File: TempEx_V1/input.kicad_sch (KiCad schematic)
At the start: 7 parts, among them J1 Conn_01x02, U1 MAX31865xTP

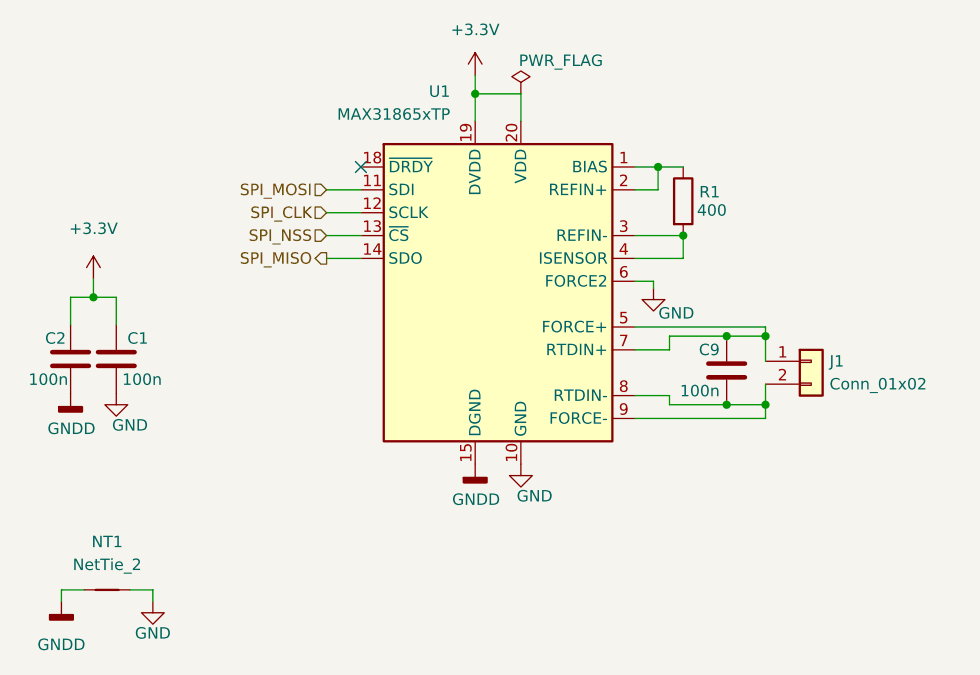
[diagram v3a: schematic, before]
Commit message: Updated GND
All GNDD switched to GND
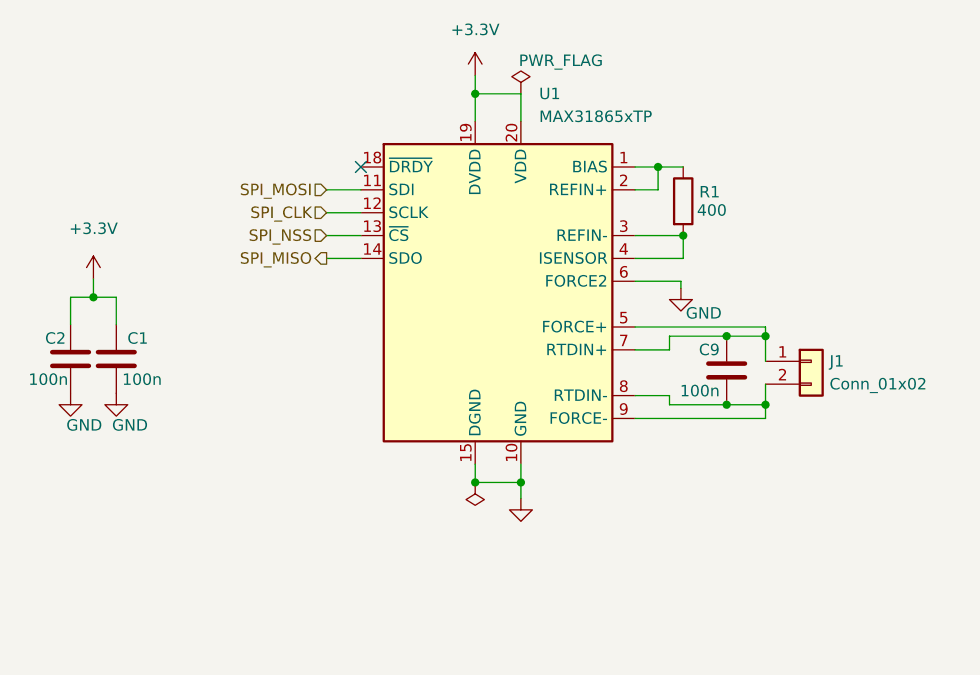
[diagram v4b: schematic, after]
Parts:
- removed NT1: NetTie_2, symbol Device:NetTie_2
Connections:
- net GNDD is gone; now on net GND: C2.2, U1.15 (DGND)

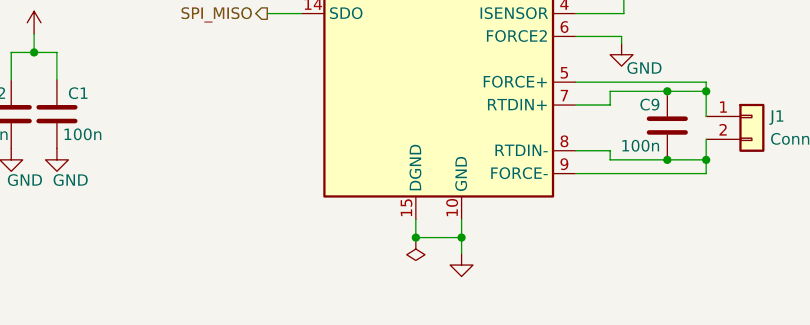
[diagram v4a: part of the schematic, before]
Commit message: Change from 2 layers to 4
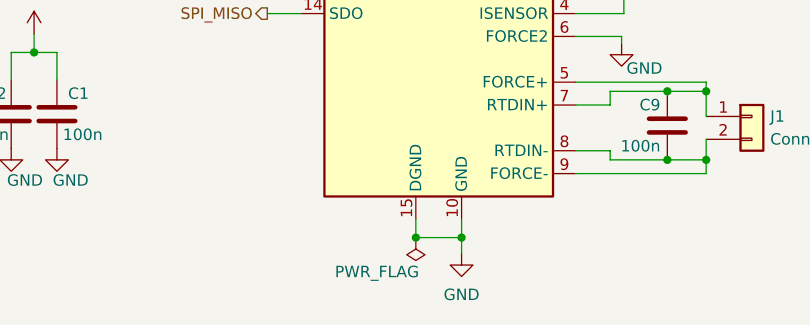
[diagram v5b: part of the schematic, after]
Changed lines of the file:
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@@
       (effects (font (size 1.27 1.27)) hide)
     )
-    (property "Value" "" (id 1) (at 182.118 123.19 0))
+    (property "Value" "GND" (id 1) (at 182.118 123.19 0))
     (property "Footprint" "" (id 2) (at 182.118 118.618 0)
       (effects (font (size 1.27 1.27)) hide)
@@
       (effects (font (size 1.27 1.27)) hide)
     )
-    (property "Value" "" (id 1) (at 172.72 120.65 0))
+    (property "Value" "PWR_FLAG" (id 1) (at 172.72 120.65 0))
     (property "Footprint" "" (id 2) (at 177.038 116.84 0)
       (effects (font (size 1.27 1.27)) hide)

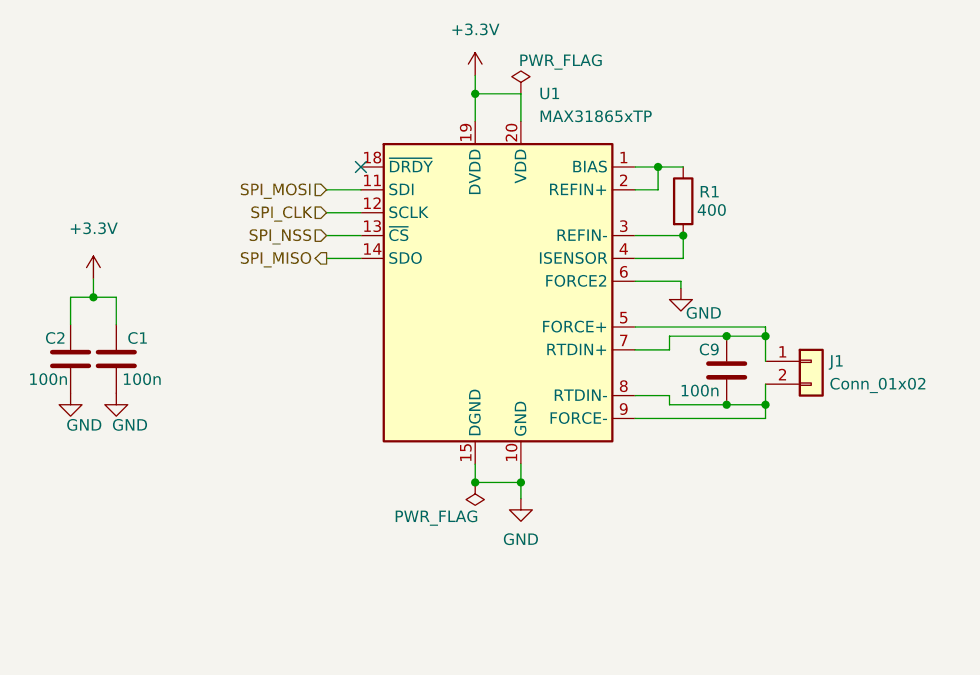
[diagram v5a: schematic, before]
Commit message: Layer change + 4 pin setup + stitching
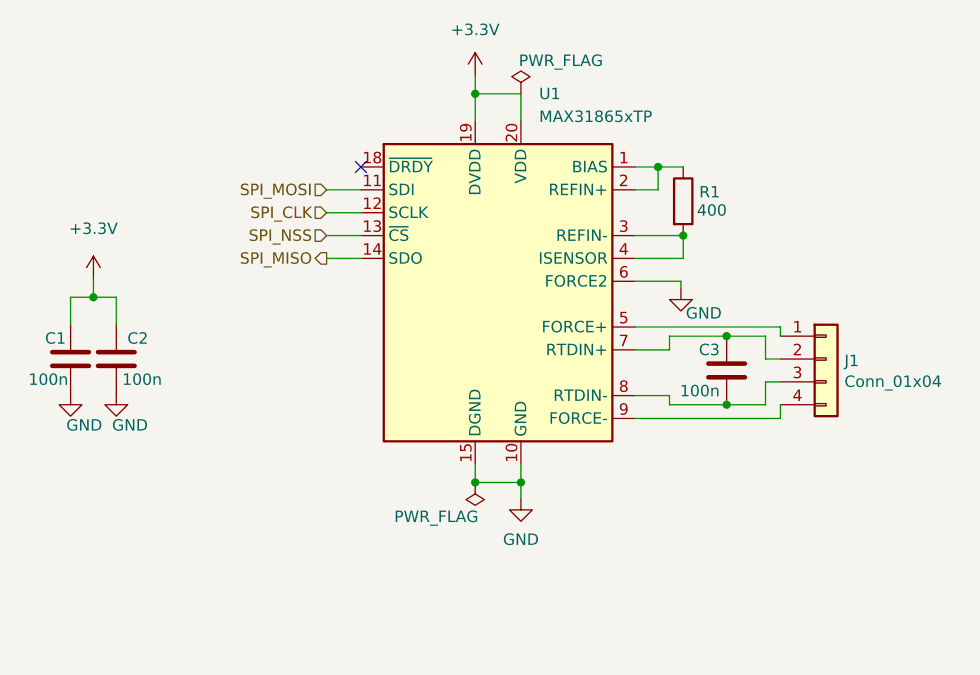
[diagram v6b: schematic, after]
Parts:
- removed J1: Conn_01x02, Connector_Molex:Molex_SL_171971-0002_1x02_P2.54mm_Vertical, symbol Connector_Generic:Conn_01x02
- added J1: Conn_01x04, TXV_Library_Footprints:TE_M12_4_Pin_PCB, symbol Connector_Generic:Conn_01x04
- renumbered C2 to C1, C1 to C2, C9 to C3
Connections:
- net at C3.1, U1.7 (RTDIN+): now also J1.2 (Pin_2); no longer U1.5 (FORCE+)
- net at C3.2, U1.8 (RTDIN-): now also J1.3 (Pin_3); no longer U1.9 (FORCE-)
- new net: J1.1 (Pin_1), U1.5 (FORCE+)
- new net: J1.4 (Pin_4), U1.9 (FORCE-)
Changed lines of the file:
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@@
   (junction (at 204.978 108.204) (diameter 0) (color 0 0 0 0)
   )
-  (junction (at 209.296 108.204) (diameter 0) (color 0 0 0 0)
-  )
-  (junction (at 209.296 100.584) (diameter 0) (color 0 0 0 0)
-  )
   (junction (at 177.038 116.84) (diameter 0) (color 0 0 0 0)
   )
@@
   )
   (no_connect (at 164.338 81.788))
-  (wire (pts (xy 209.296 109.728) (xy 209.296 108.204))
-    (stroke (width 0) (type default) (color 0 0 0 0))
-  )
   (wire (pts (xy 199.898 94.488) (xy 199.898 95.25))
     (stroke (width 0) (type default) (color 0 0 0 0))
@@
     (stroke (width 0) (type default) (color 0 0 0 0))
   )
-  (wire (pts (xy 194.818 99.568) (xy 209.296 99.568))
+  (wire (pts (xy 194.818 99.568) (xy 210.947 99.568))
     (stroke (width 0) (type default) (color 0 0 0 0))
   )
@@
     (stroke (width 0) (type default) (color 0 0 0 0))
   )
+  (wire (pts (xy 209.296 103.124) (xy 210.947 103.124))
+    (stroke (width 0) (type default) (color 0 0 0 0))
+  )
   (wire (pts (xy 194.818 81.788) (xy 197.358 81.788))
     (stroke (width 0) (type default) (color 0 0 0 0))
@@
     (stroke (width 0) (type default) (color 0 0 0 0))
   )
+  (wire (pts (xy 209.296 105.664) (xy 209.296 108.204))
+    (stroke (width 0) (type default) (color 0 0 0 0))
+  )
   (wire (pts (xy 177.038 116.84) (xy 182.118 116.84))
     (stroke (width 0) (type default) (color 0 0 0 0))
   )
-  (wire (pts (xy 209.296 100.584) (xy 209.296 103.378))
-    (stroke (width 0) (type default) (color 0 0 0 0))
-  )
   (wire (pts (xy 177.038 71.628) (xy 177.038 73.66))
     (stroke (width 0) (type default) (color 0 0 0 0))
@@
     (stroke (width 0) (type default) (color 0 0 0 0))
   )
+  (wire (pts (xy 210.947 100.584) (xy 210.947 99.568))
+    (stroke (width 0) (type default) (color 0 0 0 0))
+  )
   (wire (pts (xy 198.628 108.204) (xy 204.978 108.204))
     (stroke (width 0) (type default) (color 0 0 0 0))
@@
     (stroke (width 0) (type default) (color 0 0 0 0))
   )
-  (wire (pts (xy 209.296 99.568) (xy 209.296 100.584))
+  (wire (pts (xy 194.818 109.728) (xy 210.947 109.728))
+    (stroke (width 0) (type default) (color 0 0 0 0))
+  )
+  (wire (pts (xy 209.296 100.584) (xy 209.296 103.124))
     (stroke (width 0) (type default) (color 0 0 0 0))
   )
@@
     (stroke (width 0) (type default) (color 0 0 0 0))
   )
-  (wire (pts (xy 209.296 105.918) (xy 209.296 108.204))
-    (stroke (width 0) (type default) (color 0 0 0 0))
-  )
   (wire (pts (xy 204.978 100.584) (xy 209.296 100.584))
     (stroke (width 0) (type default) (color 0 0 0 0))
@@
     (stroke (width 0) (type default) (color 0 0 0 0))
   )
+  (wire (pts (xy 210.947 105.664) (xy 209.296 105.664))
+    (stroke (width 0) (type default) (color 0 0 0 0))
+  )
   (wire (pts (xy 182.118 116.84) (xy 182.118 114.808))
     (stroke (width 0) (type default) (color 0 0 0 0))
@@
     (stroke (width 0) (type default) (color 0 0 0 0))
   )
+  (wire (pts (xy 210.947 108.204) (xy 210.947 109.728))
+    (stroke (width 0) (type default) (color 0 0 0 0))
+  )
   (wire (pts (xy 198.628 100.584) (xy 204.978 100.584))
     (stroke (width 0) (type default) (color 0 0 0 0))
   )
   (wire (pts (xy 198.628 108.204) (xy 198.628 107.188))
-    (stroke (width 0) (type default) (color 0 0 0 0))
-  )
-  (wire (pts (xy 194.818 109.728) (xy 209.296 109.728))
     (stroke (width 0) (type default) (color 0 0 0 0))
   )
@@
     (effects (font (size 1.27 1.27)) (justify right))
   )
-  (symbol (lib_id "power:+3.3V") (at 177.038 71.628 0) (mirror y) (unit 1)
+  (symbol (lib_id "power:+3.3V") (at 177.038 71.628 0) (mirror y)
     (in_bom yes) (on_board yes) (fields_autoplaced)
-    (property "Reference" "#PWR06" (id 0) (at 177.038 75.438 0)
+    (property "Reference" "#PWR05" (id 0) (at 177.038 75.438 0)
       (effects (font (size 1.27 1.27)) hide)
     )
@@
     (pin "1")
   )
-  (symbol (lib_id "power:GND") (at 132.08 106.934 0) (mirror y) (unit 1)
-    (in_bom yes) (on_board yes)
-    (property "Reference" "#PWR07" (id 0) (at 132.08 113.284 0)
+  (symbol (lib_id "power:GND") (at 132.08 106.934 0) (mirror y)
+    (in_bom yes) (on_board yes)
+    (property "Reference" "#PWR02" (id 0) (at 132.08 113.284 0)
       (effects (font (size 1.27 1.27)) hide)
     )
@@
     (pin "1")
   )
-  (symbol (lib_id "power:GND") (at 137.16 106.934 0) (mirror y) (unit 1)
-    (in_bom yes) (on_board yes)
-    (property "Reference" "#PWR02" (id 0) (at 137.16 113.284 0)
+  (symbol (lib_id "power:GND") (at 137.16 106.934 0) (mirror y)
+    (in_bom yes) (on_board yes)
+    (property "Reference" "#PWR04" (id 0) (at 137.16 113.284 0)
       (effects (font (size 1.27 1.27)) hide)
     )
@@
     (pin "1")
   )
-  (symbol (lib_id "Device:C") (at 204.978 104.394 0) (mirror y) (unit 1)
-    (in_bom yes) (on_board yes)
-    (property "Reference" "C9" (id 0) (at 204.216 102.108 0)
+  (symbol (lib_id "Device:C") (at 204.978 104.394 0) (mirror y)
+    (in_bom yes) (on_board yes)
+    (property "Reference" "C3" (id 0) (at 204.216 102.108 0)
       (effects (font (size 1.27 1.27)) (justify left))
     )
@@
     (pin "2")
   )
-  (symbol (lib_id "Device:C") (at 137.16 103.124 0) (mirror y) (unit 1)
-    (in_bom yes) (on_board yes)
-    (property "Reference" "C1" (id 0) (at 140.716 100.838 0)
+  (symbol (lib_id "Device:C") (at 137.16 103.124 0) (mirror y)
+    (in_bom yes) (on_board yes)
+    (property "Reference" "C2" (id 0) (at 140.716 100.838 0)
       (effects (font (size 1.27 1.27)) (justify left))
     )
@@
     (pin "2")
   )
-  (symbol (lib_id "Device:C") (at 132.08 103.124 0) (mirror y) (unit 1)
-    (in_bom yes) (on_board yes)
-    (property "Reference" "C2" (id 0) (at 131.572 100.838 0)
+  (symbol (lib_id "Device:C") (at 132.08 103.124 0) (mirror y)
+    (in_bom yes) (on_board yes)
+    (property "Reference" "C1" (id 0) (at 131.572 100.838 0)
       (effects (font (size 1.27 1.27)) (justify left))
     )
@@
     (pin "2")
   )
-  (symbol (lib_id "power:GND") (at 182.118 118.618 0) (unit 1)
+  (symbol (lib_id "power:GND") (at 182.118 118.618 0)
     (in_bom yes) (on_board yes) (fields_autoplaced)
-    (property "Reference" "#PWR04" (id 0) (at 182.118 124.968 0)
+    (property "Reference" "#PWR06" (id 0) (at 182.118 124.968 0)
       (effects (font (size 1.27 1.27)) hide)
     )
@@
     (pin "1")
   )
-  (symbol (lib_id "power:GND") (at 199.898 95.25 0) (mirror y) (unit 1)
-    (in_bom yes) (on_board yes)
-    (property "Reference" "#PWR026" (id 0) (at 199.898 101.6 0)
+  (symbol (lib_id "power:GND") (at 199.898 95.25 0) (mirror y)
+    (in_bom yes) (on_board yes)
+    (property "Reference" "#PWR07" (id 0) (at 199.898 101.6 0)
       (effects (font (size 1.27 1.27)) hide)
     )
@@
     (pin "1")
   )
-  (symbol (lib_id "power:PWR_FLAG") (at 177.038 116.84 180) (unit 1)
+  (symbol (lib_id "power:PWR_FLAG") (at 177.038 116.84 180)
     (in_bom yes) (on_board yes)
     (property "Reference" "#FLG01" (id 0) (at 177.038 118.745 0)
@@
     (pin "1")
   )
-  (symbol (lib_id "Sensor_Temperature:MAX31865xTP") (at 179.578 97.028 0) (unit 1)
+  (symbol (lib_id "Sensor_Temperature:MAX31865xTP") (at 179.578 97.028 0)
     (in_bom yes) (on_board yes) (fields_autoplaced)
     (property "Reference" "U1" (id 0) (at 184.1374 73.66 0)
@@
     (pin "9")
   )
-  (symbol (lib_id "power:PWR_FLAG") (at 182.118 73.66 0) (unit 1)
-    (in_bom yes) (on_board yes)
-    (property "Reference" "#FLG0101" (id 0) (at 182.118 71.755 0)
+  (symbol (lib_id "power:PWR_FLAG") (at 182.118 73.66 0)
+    (in_bom yes) (on_board yes)
+    (property "Reference" "#FLG02" (id 0) (at 182.118 71.755 0)
       (effects (font (size 1.27 1.27)) hide)
     )
@@
     (pin "1")
   )
-  (symbol (lib_id "Connector_Generic:Conn_01x02") (at 214.376 103.378 0) (unit 1)
-    (in_bom yes) (on_board yes) (fields_autoplaced)
-    (property "Reference" "J1" (id 0) (at 216.408 103.3779 0)
-      (effects (font (size 1.27 1.27)) (justify left))
-    )
-    (property "Value" "Conn_01x02" (id 1) (at 216.408 105.9179 0)
-      (effects (font (size 1.27 1.27)) (justify left))
-    )
-    (property "Footprint" "Connector_Molex:Molex_SL_171971-0002_1x02_P2.54mm_Vertical" (id 2) (at 214.376 103.378 0)
-      (effects (font (size 1.27 1.27)) hide)
-    )
-    (property "Datasheet" "~" (id 3) (at 214.376 103.378 0)
-      (effects (font (size 1.27 1.27)) hide)
-    )
-    (pin "1")
-    (pin "2")
-  )
-  (symbol (lib_id "power:+3.3V") (at 134.62 94.234 0) (mirror y) (unit 1)
+  (symbol (lib_id "Connector_Generic:Conn_01x04") (at 216.027 103.124 0)
+    (in_bom yes) (on_board yes)
+    (property "Reference" "J1" (id 0) (at 218.059 103.3272 0)
+      (effects (font (size 1.27 1.27)) (justify left))
+    )
+    (property "Value" "Conn_01x04" (id 1) (at 218.059 105.6386 0)
+      (effects (font (size 1.27 1.27)) (justify left))
+    )
+    (property "Footprint" "TXV_Library_Footprints:TE_M12_4_Pin_PCB" (id 2) (at 216.027 103.124 0)
+      (effects (font (size 1.27 1.27)) hide)
+    )
+    (property "Datasheet" "~" (id 3) (at 216.027 103.124 0)
+      (effects (font (size 1.27 1.27)) hide)
+    )
+    (pin "1")
+    (pin "2")
+    (pin "3")
+    (pin "4")
+  )
+  (symbol (lib_id "power:+3.3V") (at 134.62 94.234 0) (mirror y)
     (in_bom yes) (on_board yes) (fields_autoplaced)
     (property "Reference" "#PWR03" (id 0) (at 134.62 98.044 0)
@@
     (pin "1")
   )
-  (symbol (lib_id "Device:R") (at 200.152 85.598 0) (unit 1)
+  (symbol (lib_id "Device:R") (at 200.152 85.598 0)
     (in_bom yes) (on_board yes)
     (property "Reference" "R1" (id 0) (at 201.93 84.582 0)
